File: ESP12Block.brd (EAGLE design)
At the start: 100 x 80 mm, 16 parts, among them U1 TPS5410DR

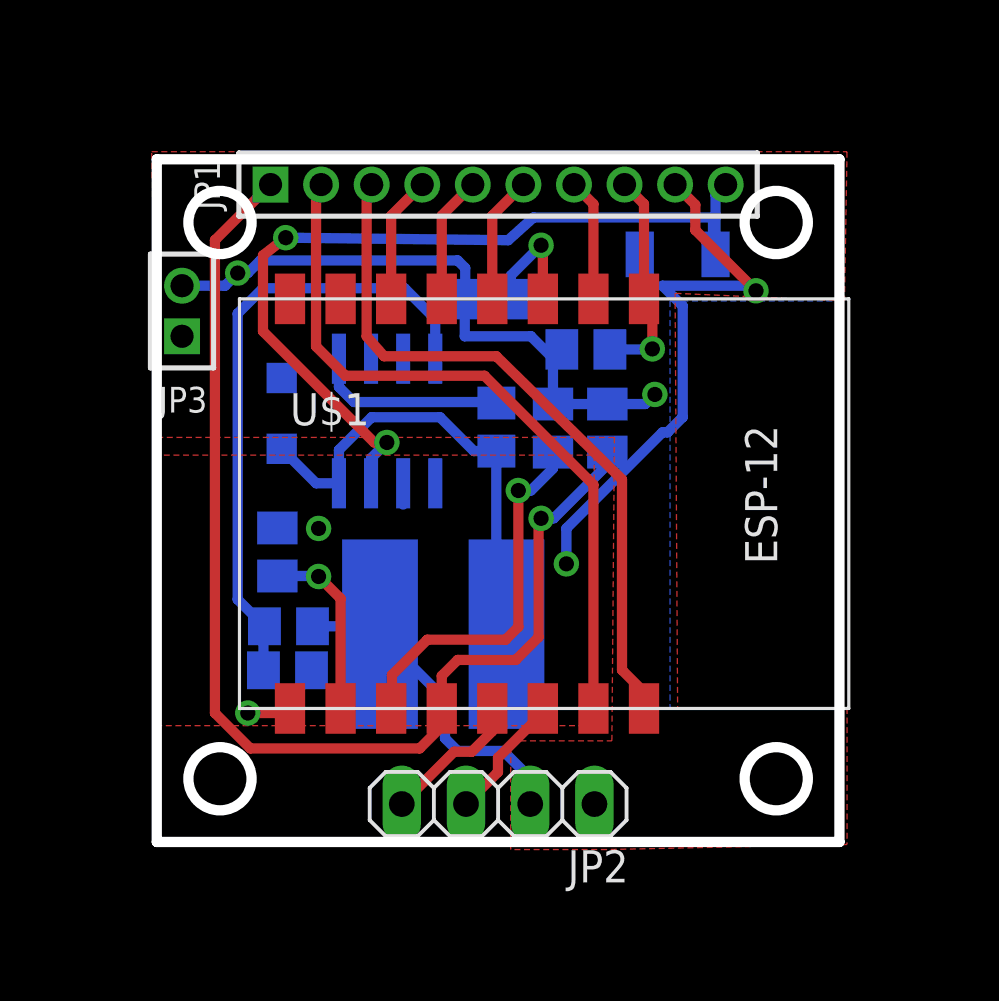
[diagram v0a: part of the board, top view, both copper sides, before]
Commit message: trying a different orientation
doesn't quite work out for the 3V3 rail
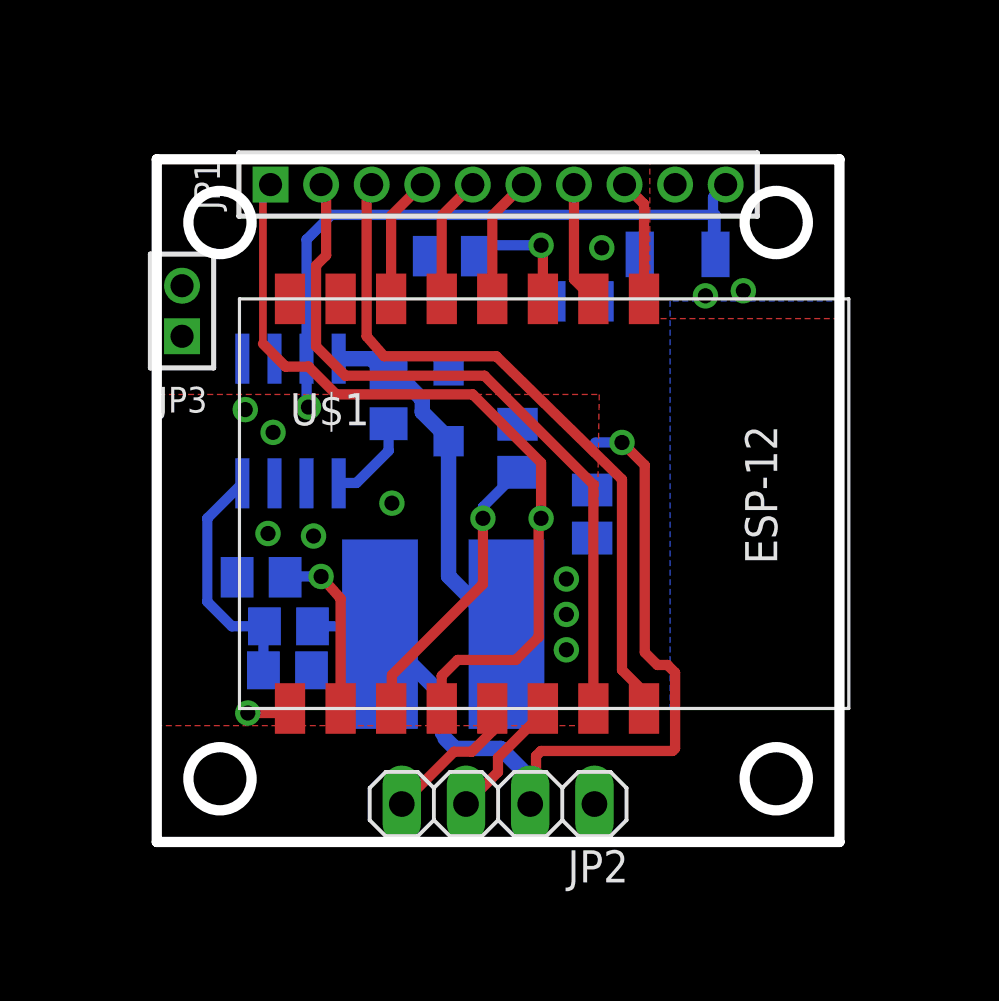
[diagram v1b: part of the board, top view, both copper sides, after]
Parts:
- moved D1 6.61 mm to (21.5, 27.2)
- moved C4 4.39 mm to (19.2, 27.5), turned to 90 degrees
- moved U1 3.82 mm to (15.3, 26.6), turned to 90 degrees
- moved R2 3.45 mm to (27.2, 23.0)
- moved R1 2.20 mm to (21.7, 33.2)
- moved R4 1.96 mm to (26.5, 31.4)
- moved R3 1.61 mm to (24.3, 25.6)
- moved R5 1.19 mm to (14.1, 20.5), turned to 180 degrees
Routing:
- net GND: track 25.2 -> 1.74 mm, vias 4 -> 11
- net SENS: track 24.9 -> 9.68 mm
- net GPIO0: track 47.0 -> 33.0 mm
- net +12V: track 34.6 -> 27.8 mm, vias 2 -> 1
- net BOOT: track 7.61 -> 3.58 mm
- net PH: track 19.1 -> 15.3 mm
- net GPIO2: track 14.9 -> 11.4 mm
- net RST: track 8.64 -> 5.66 mm
- net +3V3: track 37.8 -> 35.6 mm, vias 2 -> 1
- removed copper zone on layer 1, net +3V3
